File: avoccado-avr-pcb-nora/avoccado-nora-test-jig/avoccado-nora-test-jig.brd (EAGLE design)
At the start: 25 x 24.5 mm, 30 parts, among them J1 AVR_SPI_PROG2PTH2

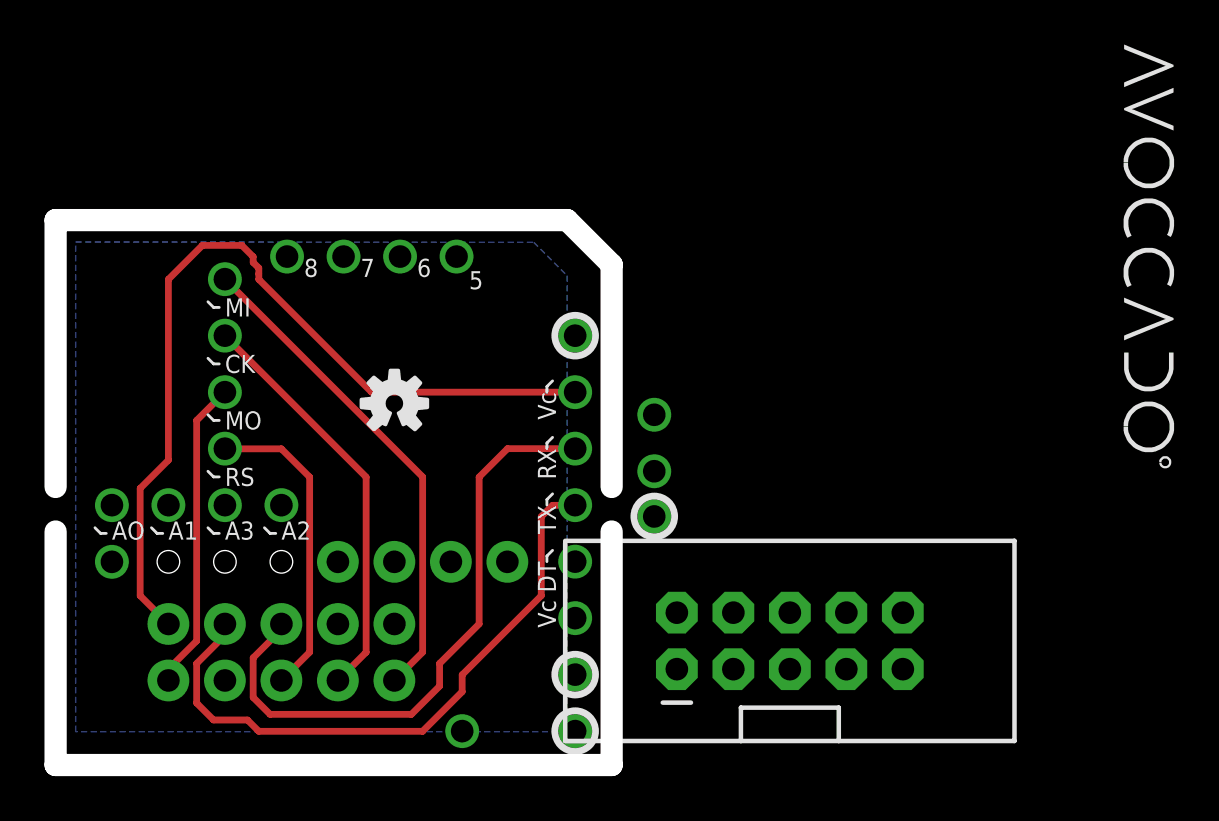
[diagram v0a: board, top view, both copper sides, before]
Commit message: switch layer for ICSP 2x5 header to bottom
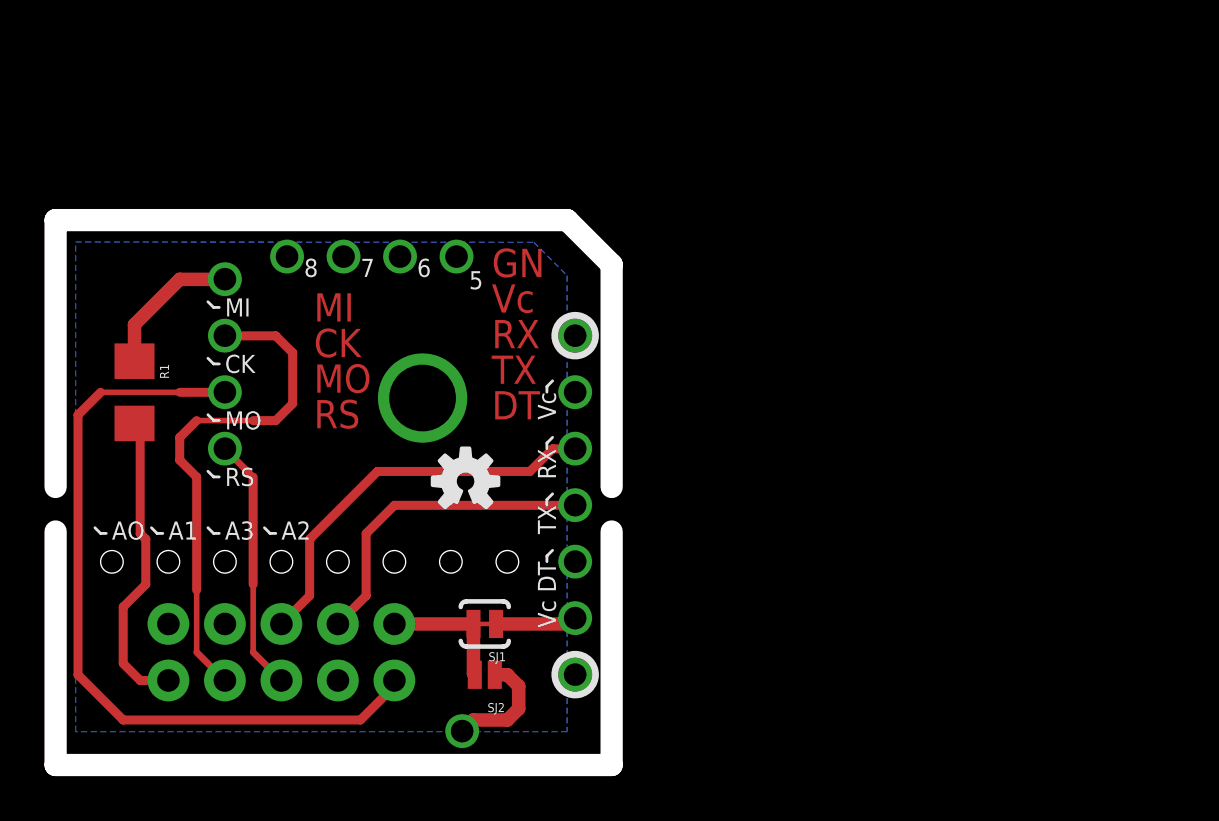
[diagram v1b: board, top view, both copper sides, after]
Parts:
- removed J1: AVR_SPI_PROG2PTH2, SparkFun-Connectors:2X5-SHROUDED
- removed JP19, JP20, JP21, JP22, JP23, JP24, JP25, JP26, TP2: M01NOSILK-KIT, SparkFun-Connectors:1X01NS-KIT
- removed JP4, JP5: M021X02_NO_SILK, SparkFun-Connectors:1X02_NO_SILK
- added R1: 0, SparkFun-Passives:1206
- added SJ1: JUMPER-PAD-2-NC_BY_TRACE, SparkFun-Passives:PAD-JUMPER-2-NC_BY_TRACE_YES_SILK
- added SJ2: JUMPER-PAD-2-NO, SparkFun-Passives:PAD-JUMPER-2-NO_NO_SILK
- moved LOGO2 4.74 mm to (17.9, 12.3)
- flipped ICSP to the bottom
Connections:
- removed net A0: JP19.1
- removed net A1: JP20.1
- removed net A2: JP21.1
- removed net A3: JP22.1
- removed net A4: JP5.2
- removed net A5: JP5.1
- removed net D2: TP2.1
- removed net VBAT: JP24.1
- removed net VCC: J1.2
- removed net VIBR: JP23.1
- new net MISO1: ICSP.9, R1.2
- new net VTG: ICSP.2, SJ1.2, SJ2.2
- net 3.3V: now also SJ1.1; no longer ICSP.2, JP4.1
- net 5V: now also SJ2.1
- net GND: no longer J1.10, J1.4, J1.6, J1.8, JP25.1, JP26.1, JP4.2
- net MISO: now also R1.1; no longer ICSP.9
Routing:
- net 3.3V: track 38.6 -> 3.66 mm
- net MOSI: track 14.0 -> 34.7 mm
- net MISO: track 22.3 -> 6.56 mm
- net TXO: track 28.4 -> 14.5 mm
- net MISO1: track 0.00 -> 13.8 mm
- net RXI: track 28.0 -> 17.9 mm
- net VTG: track 0.00 -> 5.87 mm
- net 5V: track 0.00 -> 5.26 mm
- net SCK: track 18.7 -> 23.1 mm
- net RESET: track 14.0 -> 11.5 mm
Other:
- board text added: "GN"
- board text added: "TEST JIG FOR AVOCCADO NORA 2 SHURE OPEN TECHNOLOGIES"
- board text removed: "3.3V 3.6-4.2V 5-5.5V"
- board text removed: "AVOCCADO NORA 2 SHURE OPEN TECHNOLOGIES ETEMU.COM 2015"
- board text removed: "Vc Vb Vi"

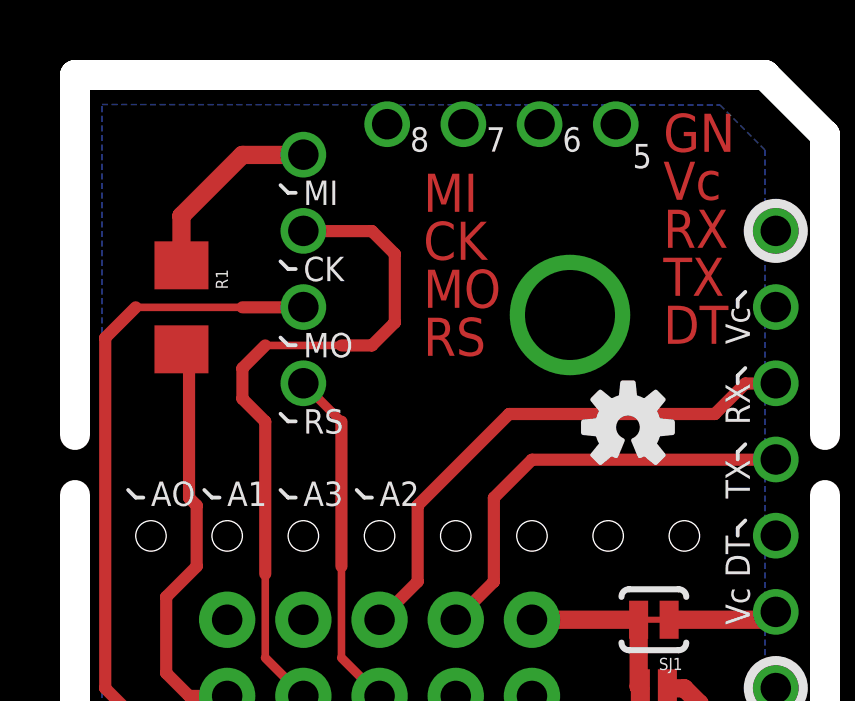
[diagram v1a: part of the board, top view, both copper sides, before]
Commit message: ditch DTR line at ICSP header
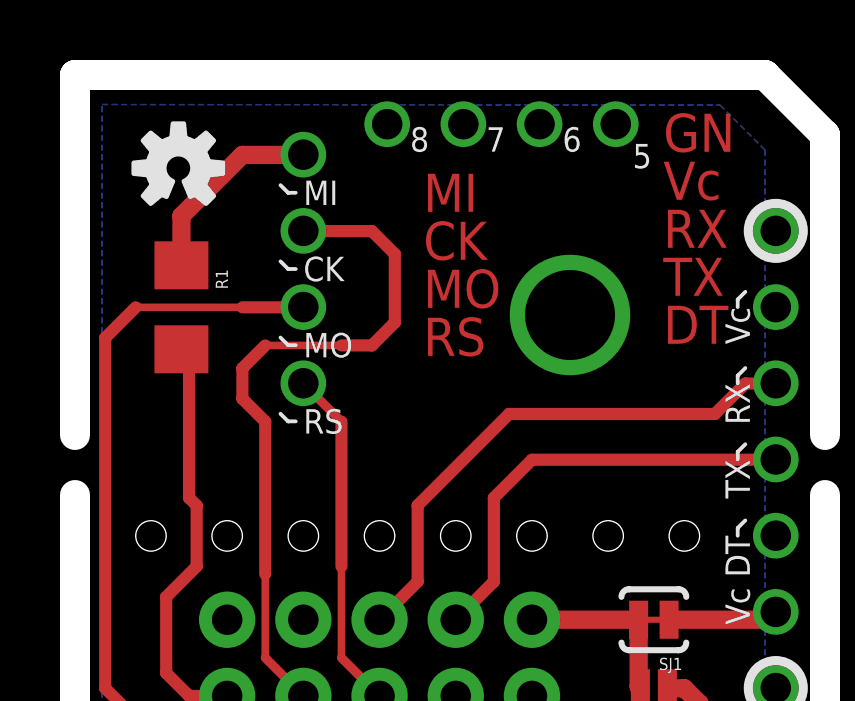
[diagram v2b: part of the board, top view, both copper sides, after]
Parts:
- moved LOGO2 17.3 mm to (2.95, 20.9)
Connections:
- net DTR: no longer ICSP.8
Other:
- board text removed: "A1"
- board text removed: "A2"
- board text removed: "A3"
- board text removed: "AO"

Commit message: pour gnd
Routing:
- net SCK: track 23.1 -> 22.1 mm
- added copper zone on layer 1, net GND
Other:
- board text added: "AVOCCADO NORA 2 JIG SHURE OPEN TECHNOLOGIES 2015"
- board text added: "GND"
- board text added: "R"
- board text removed: "GN"
- board text removed: "TEST JIG FOR AVOCCADO NORA 2 SHURE OPEN TECHNOLOGIES"
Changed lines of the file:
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@@
 <setting verticaltext="up"/>
 </settings>
-<grid distance="0.02" unitdist="inch" unit="inch" style="lines" multiple="1" display="yes" altdistance="0.01" altunitdist="inch" altunit="inch"/>
+<grid distance="1" unitdist="mm" unit="mm" style="lines" multiple="1" display="yes" altdistance="0.1" altunitdist="mm" altunit="mm"/>
 <layers>
 <layer number="1" name="Top" color="5" fill="1" visible="yes" active="yes"/>
@@
 <wire x1="21.59" y1="8.898" x2="21.844" y2="9.152" width="0.127" layer="21"/>
 <wire x1="21.59" y1="8.644" x2="21.59" y2="8.898" width="0.127" layer="21"/>
-<text x="21.59" y="6.912" size="0.8128" layer="21" ratio="10" rot="SR90" align="center-right">Vc</text>
 <text x="21.59" y="16.264" size="0.8128" layer="21" ratio="10" rot="SR90" align="center-right">Vc</text>
 <wire x1="21.59" y1="16.518" x2="21.844" y2="16.772" width="0.127" layer="21"/>
 <wire x1="21.59" y1="16.264" x2="21.59" y2="16.518" width="0.127" layer="21"/>
-<text x="20.336" y="13.745" size="0.8128" layer="22" font="vector" ratio="10" rot="MR0" align="top-left">TEST JIG FOR
-AVOCCADO NORA 2
-SHURE OPEN
-TECHNOLOGIES</text>
+<text x="20.844" y="11.459" size="0.8128" layer="22" font="vector" ratio="10" rot="MR0" align="top-left">AVOCCADO NORA 2 JIG
+SHURE OPEN TECHNOLOGIES 2015</text>
 <circle x="22.86" y="3.564" radius="0.915809375" width="0.3048" layer="22"/>
 <circle x="22.86" y="3.564" radius="0.915809375" width="0.3048" layer="21"/>
@@
 <hole x="19.812" y="8.636" drill="1.016"/>
 <hole x="2.032" y="8.636" drill="1.016"/>
-<text x="11.112" y="20.074" size="1.27" layer="1" font="vector" ratio="15" rot="SR0" align="center-left">MI</text>
-<text x="11.112" y="18.474" size="1.27" layer="1" font="vector" ratio="15" rot="SR0" align="center-left">CK</text>
-<text x="11.112" y="16.874" size="1.27" layer="1" font="vector" ratio="15" rot="SR0" align="center-left">MO</text>
-<text x="11.112" y="15.274" size="1.27" layer="1" font="vector" ratio="15" rot="SR0" align="center-left">RS</text>
-<text x="19.112" y="22.074" size="1.27" layer="1" font="vector" ratio="15" rot="SR0" align="center-left">GN</text>
-<text x="19.112" y="20.474" size="1.27" layer="1" font="vector" ratio="15" rot="SR0" align="center-left">Vc</text>
-<text x="19.112" y="18.874" size="1.27" layer="1" font="vector" ratio="15" rot="SR0" align="center-left">RX</text>
-<text x="19.112" y="17.274" size="1.27" layer="1" font="vector" ratio="15" rot="SR0" align="center-left">TX</text>
-<text x="19.112" y="15.674" size="1.27" layer="1" font="vector" ratio="15" rot="SR0" align="center-left">DT</text>
+<text x="11.366" y="19.566" size="1.27" layer="41" font="vector" ratio="13" rot="SR0" align="center-left">MI</text>
+<text x="11.366" y="17.966" size="1.27" layer="41" font="vector" ratio="13" rot="SR0" align="center-left">CK</text>
+<text x="11.366" y="16.366" size="1.27" layer="41" font="vector" ratio="13" rot="SR0" align="center-left">MO</text>
+<text x="11.366" y="14.766" size="1.27" layer="41" font="vector" ratio="13" rot="SR0" align="center-left">R</text>
+<rectangle x1="3.048" y1="3.048" x2="14.732" y2="7.112" layer="41"/>
+<text x="19.812" y="2.548" size="0.8128" layer="21" ratio="10" rot="SR90" align="center-right">Vi</text>
+<wire x1="19.566" y1="0.762" x2="19.82" y2="1.016" width="0.127" layer="21"/>
+<wire x1="18.804" y1="0.762" x2="19.566" y2="0.762" width="0.127" layer="21"/>
+<text x="21.59" y="6.104" size="0.8128" layer="21" ratio="10" rot="SR90" align="center-right">Vc</text>
+<wire x1="21.59" y1="6.358" x2="21.844" y2="6.612" width="0.127" layer="21"/>
+<wire x1="21.59" y1="6.104" x2="21.59" y2="6.358" width="0.127" layer="21"/>
+<text x="21.59" y="22.868" size="0.8128" layer="21" ratio="10" rot="SR90" align="center-right">GND</text>
+<wire x1="21.59" y1="20.074" x2="21.844" y2="19.82" width="0.127" layer="21"/>
+<wire x1="21.59" y1="20.328" x2="21.59" y2="20.074" width="0.127" layer="21"/>
+<text x="21.59" y="3.056" size="0.8128" layer="21" ratio="10" rot="SR90" align="center-right">GND</text>
+<wire x1="21.59" y1="3.31" x2="21.844" y2="3.564" width="0.127" layer="21"/>
+<wire x1="21.59" y1="3.056" x2="21.59" y2="3.31" width="0.127" layer="21"/>
+<text x="4.572" y="12.2" size="0.8128" layer="21" ratio="10" rot="SR90" align="center-right">GND</text>
+<text x="14.732" y="11.438" size="0.8128" layer="21" ratio="10" rot="SR90" align="center-right">Vc</text>
+<text x="9.644" y="0.508" size="0.8128" layer="21" ratio="10" rot="SR90" align="center-left">RS</text>
+<text x="14.724" y="0.508" size="0.8128" layer="21" ratio="10" rot="SR90" align="center-left">MO</text>
+<text x="7.104" y="0.508" size="0.8128" layer="21" ratio="10" rot="SR90" align="center-left">CK</text>
+<text x="4.564" y="0.508" size="0.8128" layer="21" ratio="10" rot="SR90" align="center-left">MI</text>
+<text x="9.652" y="11.438" size="0.8128" layer="21" ratio="10" rot="SR90" align="center-right">RX</text>
+<text x="12.192" y="11.438" size="0.8128" layer="21" ratio="10" rot="SR90" align="center-right">TX</text>
 </plain>
 <attributes>
@@
 <element name="LOGO2" library="SparkFun-Aesthetics" package="OSHW-LOGO-S" value="OSHW-LOGOS" x="2.946" y="20.892"/>
 <element name="ICSP" library="SparkFun-Connectors" package="2X5_NOSILK" value="M05X2NO_SILK" x="9.652" y="4.572" smashed="yes" rot="MR90"/>
-<element name="SJ1" library="SparkFun-Passives" package="PAD-JUMPER-2-NC_BY_TRACE_YES_SILK" value="JUMPER-PAD-2-NC_BY_TRACE" x="18.796" y="5.842" rot="R180"/>
-<element name="SJ2" library="SparkFun-Passives" package="PAD-JUMPER-2-NO_NO_SILK" value="JUMPER-PAD-2-NO" x="18.796" y="3.556" rot="R180"/>
+<element name="SJ1" library="SparkFun-Passives" package="PAD-JUMPER-2-NC_BY_TRACE_YES_SILK" value="JUMPER-PAD-2-NC_BY_TRACE" x="18.796" y="5.842" smashed="yes" rot="R180"/>
+<element name="SJ2" library="SparkFun-Passives" package="PAD-JUMPER-2-NO_NO_SILK" value="JUMPER-PAD-2-NO" x="18.796" y="3.556" smashed="yes" rot="R180"/>
 <element name="R1" library="SparkFun-Passives" package="1206" value="0" x="3.048" y="16.256" rot="R270"/>
 </elements>
 <signals>
 <signal name="GND" class="1">
-<polygon width="0.2032" layer="16" isolate="0.2794">
+<polygon width="0.2032" layer="16" isolate="0.6096">
 <vertex x="0.4" y="23.016"/>
 <vertex x="21" y="23"/>
@@
 <contactref element="JP3" pad="1"/>
 <contactref element="ICSP" pad="10"/>
+<polygon width="0.4064" layer="1" isolate="0.6096" orphans="yes">
+<vertex x="0" y="0"/>
+<vertex x="0" y="25"/>
+<vertex x="25" y="25"/>
+<vertex x="25" y="0"/>
+</polygon>
+<polygon width="0.127" layer="1" orphans="yes">
+<vertex x="10.414" y="13.208"/>
+<vertex x="10.414" y="20.828"/>
+<vertex x="14.732" y="20.828"/>
+<vertex x="14.732" y="13.97"/>
+<vertex x="13.716" y="13.97"/>
+<vertex x="12.7" y="13.208"/>
+</polygon>
+<via x="17" y="17" extent="1-16" drill="3" diameter="4" alwaysstop="yes"/>
+<polygon width="0.4064" layer="16" isolate="0.6096">
+<vertex x="25" y="0"/>
+<vertex x="25" y="25"/>
+<vertex x="0" y="25"/>
+<vertex x="0" y="0"/>
+</polygon>
 </signal>
 <signal name="RESET">
@@
 <wire x1="5.08" y1="13.208" x2="5.08" y2="14.224" width="0.4064" layer="1"/>
 <wire x1="5.08" y1="14.224" x2="5.842" y2="14.986" width="0.4064" layer="1"/>
-<wire x1="9.398" y1="14.986" x2="10.16" y2="15.748" width="0.4064" layer="1"/>
-<wire x1="10.16" y1="15.748" x2="10.16" y2="18.034" width="0.4064" layer="1"/>
-<wire x1="10.16" y1="18.034" x2="9.398" y2="18.796" width="0.4064" layer="1"/>
-<wire x1="9.398" y1="18.796" x2="7.12" y2="18.796" width="0.4064" layer="1"/>
+<wire x1="8.89" y1="14.986" x2="9.652" y2="15.748" width="0.4064" layer="1"/>
+<wire x1="9.652" y1="15.748" x2="9.652" y2="18.034" width="0.4064" layer="1"/>
+<wire x1="9.652" y1="18.034" x2="8.89" y2="18.796" width="0.4064" layer="1"/>
+<wire x1="8.89" y1="18.796" x2="7.12" y2="18.796" width="0.4064" layer="1"/>
 <wire x1="7.12" y1="18.796" x2="7.112" y2="18.804" width="0.3048" layer="1"/>
 <wire x1="5.842" y1="4.572" x2="5.842" y2="7.366" width="0.254" layer="1"/>
 <wire x1="5.842" y1="7.366" x2="5.842" y2="12.446" width="0.4064" layer="1"/>
-<wire x1="9.398" y1="14.986" x2="8.382" y2="14.986" width="0.4064" layer="1"/>
+<wire x1="8.89" y1="14.986" x2="8.382" y2="14.986" width="0.4064" layer="1"/>
 <wire x1="8.382" y1="14.986" x2="5.842" y2="14.986" width="0.254" layer="1"/>
 </signal>
@@
 <wire x1="3.302" y1="14.602" x2="3.048" y2="14.856" width="0.3048" layer="1"/>
 </signal>
-<signal name="N$1">
-<via x="16" y="16" extent="1-16" drill="3" diameter="4"/>
-</signal>
 </signals>
